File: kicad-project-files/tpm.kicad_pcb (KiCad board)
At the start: 2 copper layers, 25 x 13.2 mm, 11 parts, among them J1 SLB9665 header, U1 SLB9665

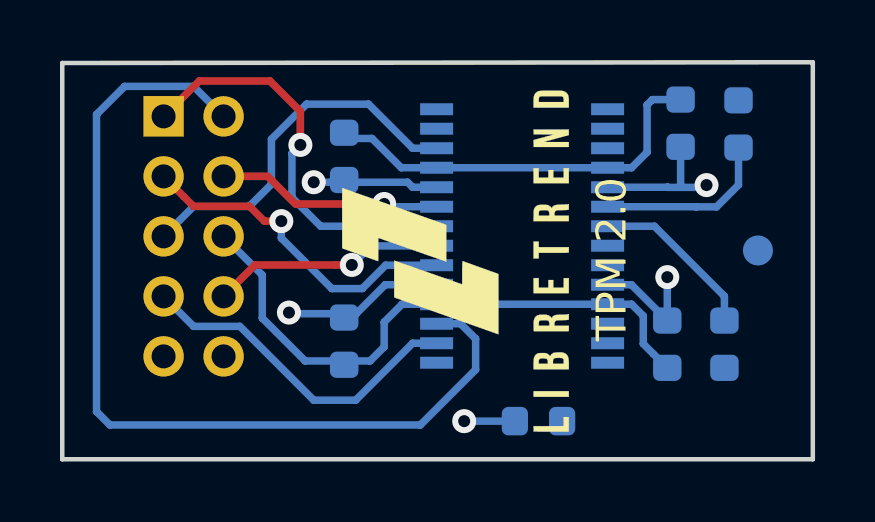
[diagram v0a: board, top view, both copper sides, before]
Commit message: Shorted +3v3 pins
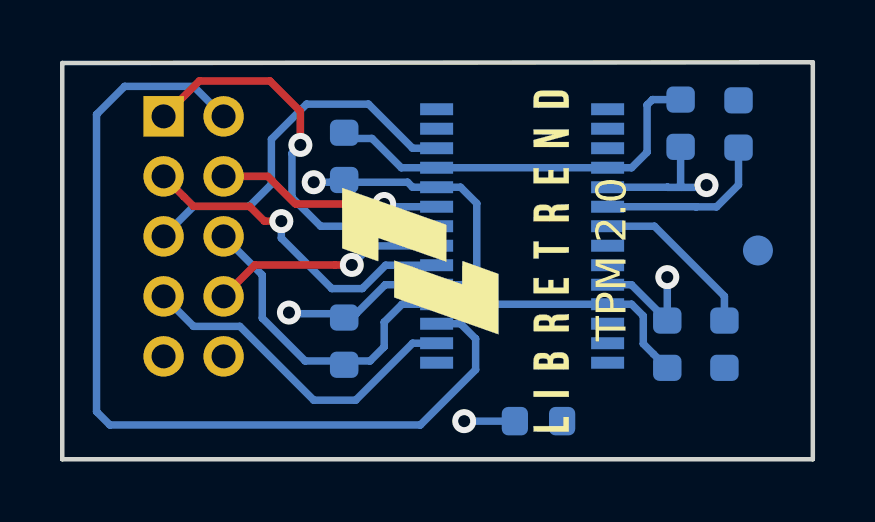
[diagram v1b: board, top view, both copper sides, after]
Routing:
- net +3V3: track 20.3 -> 25.7 mm
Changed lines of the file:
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@@
-(kicad_pcb (version 20171130) (host pcbnew 5.0.0-fee4fd1~66~ubuntu18.04.1)
+(kicad_pcb (version 20171130) (host pcbnew 5.0.1-33cea8e~67~ubuntu18.04.1)
   (general
     (thickness 1.6)
     (drawings 5)
-    (tracks 124)
+    (tracks 129)
     (zones 0)
     (modules 11)
@@
     (pad_drill 0.762)
     (pad_to_mask_clearance 0.2)
+    (solder_mask_min_width 0.25)
     (aux_axis_origin 0 0)
     (visible_elements FFFFFF7F)
@@
   (via (at 130.7846 102.1334) (size 0.8) (drill 0.4) (layers F.Cu B.Cu) (net 1))
   (segment (start 130.7846 103.5811) (end 130.7846 102.1334) (width 0.25) (layer B.Cu) (net 1))
+  (segment (start 123.8959 99.1368) (end 124.4346 99.6755) (width 0.25) (layer B.Cu) (net 1))
+  (segment (start 123.0959 99.1368) (end 123.8959 99.1368) (width 0.25) (layer B.Cu) (net 1))
+  (segment (start 124.4346 99.6755) (end 124.4346 101.9302) (width 0.25) (layer B.Cu) (net 1))
+  (segment (start 123.978 102.3868) (end 123.0959 102.3868) (width 0.25) (layer B.Cu) (net 1))
+  (segment (start 124.4346 101.9302) (end 123.978 102.3868) (width 0.25) (layer B.Cu) (net 1))
   (segment (start 129.5959 98.4868) (end 130.1115 97.9712) (width 0.25) (layer B.Cu) (net 2))
   (segment (start 128.7959 98.4868) (end 129.5959 98.4868) (width 0.25) (layer B.Cu) (net 2))
